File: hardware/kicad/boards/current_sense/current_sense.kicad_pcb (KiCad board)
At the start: 2 copper layers, 120 x 80 mm, 17 parts, among them J1 kanal 1 retur, J2 kanal 2 retur, J3 kanal 3 retur, J4 Arduino, U1 LM358, U2 LM358

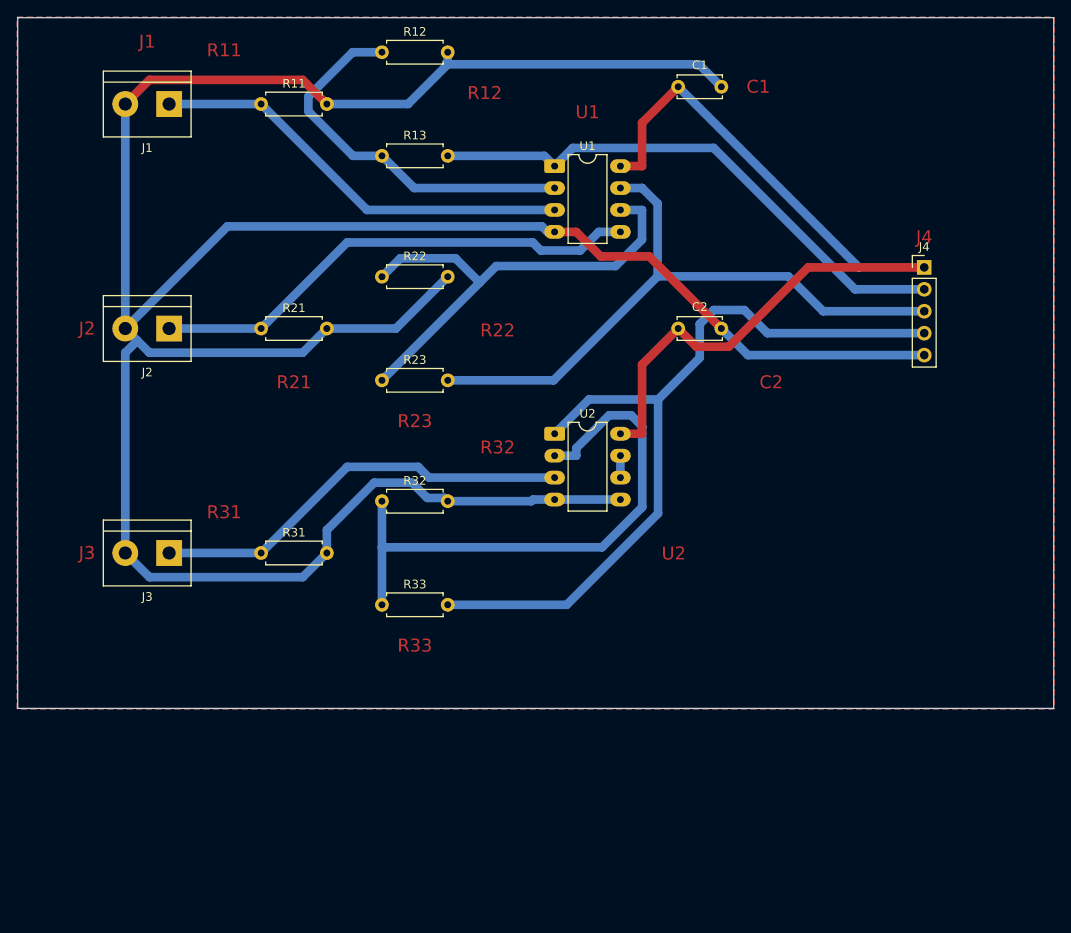
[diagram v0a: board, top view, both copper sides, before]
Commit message: Move all boards to the 104x104 jig format with compact placement
The laser positioning jig takes an exactly 109x109 mm copper blank, so every
board now has identical 104x104 edge cuts (2.5 mm rim). pcb_build.py:
- fixed JIG_W/JIG_H outline, hard failure if content overflows the square
- compact packing: 5 mm bbox gaps (was 8), squarish component cluster below
  the connector zone instead of full-width rows
- mppt/current_sense PLACE layouts re-arranged for the square and tightened

All 7 boards rerouted: 0 unconnected, 0 real DRC errors, and no vias needed
anywhere (the square format routes better than the old elongated boards).
Production DXF/gerbers re-exported; README run-plan updated for the jig
(cut blanks to exactly 109x109, all boards share the same size now).
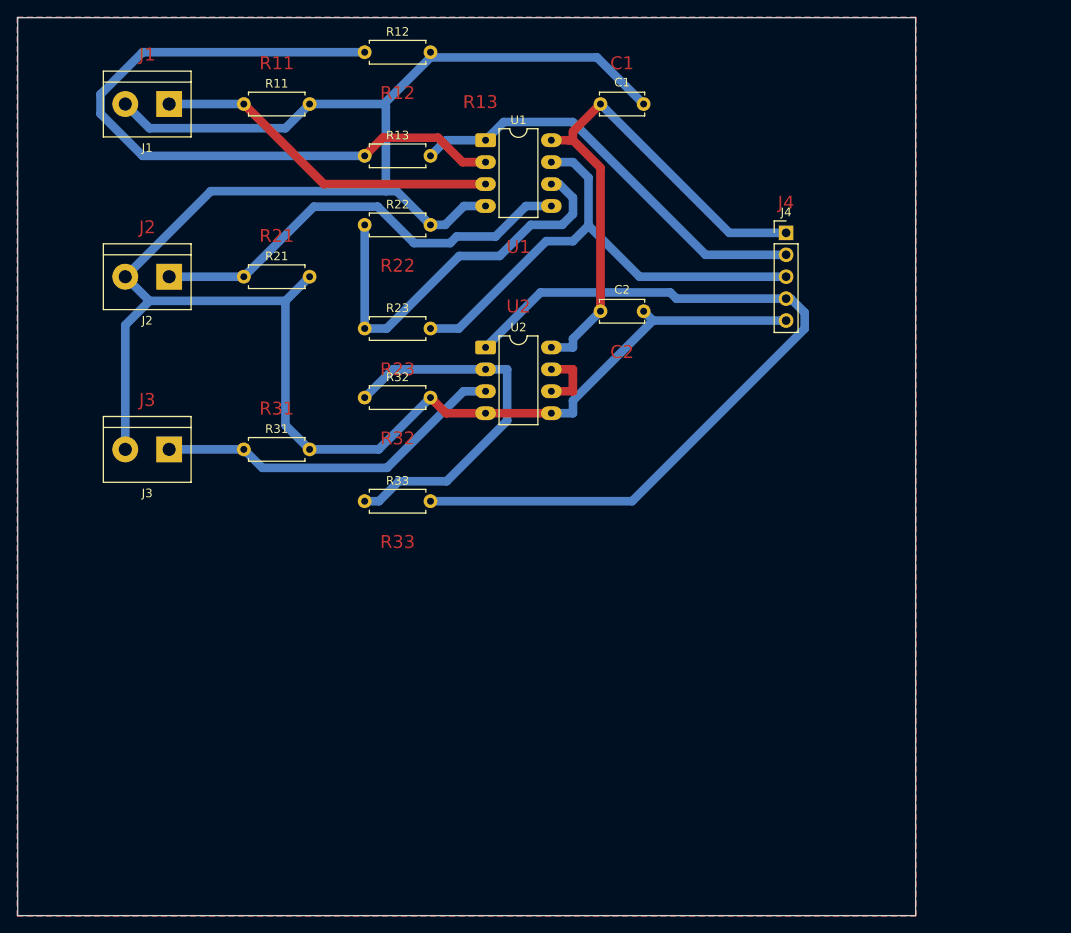
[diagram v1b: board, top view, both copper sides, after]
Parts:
- moved J4 16.5 mm to (109.0, 44.9)
- moved U2 12.8 mm to (74.2, 58.2)
- moved R31 12.2 mm to (46.2, 70.0)
- moved R32 12.2 mm to (60.2, 64.0)
- moved R33 12.2 mm to (60.2, 76.0)
- moved J3 12.0 mm to (37.5, 70.0)
- moved C1 9.22 mm to (87.5, 30.0)
- moved C2 9.22 mm to (87.5, 54.0)
- moved U1 8.54 mm to (74.2, 34.2)
- moved R21 6.32 mm to (46.2, 50.0)
- moved R22 6.32 mm to (60.2, 44.0)
- moved R23 6.32 mm to (60.2, 56.0)
- moved J2 6.00 mm to (37.5, 50.0)
- moved R11 2.00 mm to (46.2, 30.0)
- moved R12 2.00 mm to (60.2, 24.0)
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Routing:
- net GND: track 338.3 -> 251.6 mm
- net /FB1: track 44.6 -> 83.5 mm
- net +5V: track 100.2 -> 64.8 mm
- net /FB3: track 66.5 -> 44.2 mm
- net /I_SENSE2: track 75.3 -> 59.2 mm
- net /I_SENSE1: track 63.3 -> 49.2 mm
- net /FB2: track 56.2 -> 46.7 mm
- net /RET1: track 49.7 -> 40.5 mm
- net /RET3: track 49.3 -> 41.2 mm
- net /RET2: track 57.7 -> 51.2 mm
- net /U2B_FB: track 2.54 -> 7.54 mm
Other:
- board size 120 x 80 mm -> 104 x 104 mm
- board text added: "R13"

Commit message: Condense and center all boards in the jig outline; reroute drive_circuit
Placement (pcb_build.py): connector columns now hug the component block
instead of sitting at the board edges, and the whole cluster is translated to
the center of the 104x104 outline - nothing sits next to the edge cuts
anymore. Fail-hard check if a cluster outgrows the jig.

drive_circuit keeps the hand-made GUI placement but is rerouted with the
two-stage flow: 43 top tracks + 1 via from the GUI autoroute down to 20
pin-to-pin bridges, no via. New tools/strip_routing.py removes existing
routing textually (sexpdata) - in-process pcbnew Remove() access-violates.

All 7 boards: 0 unconnected, 0 real DRC errors, no vias anywhere; buck is
now fully single-sided (0 top tracks). Production files re-exported.
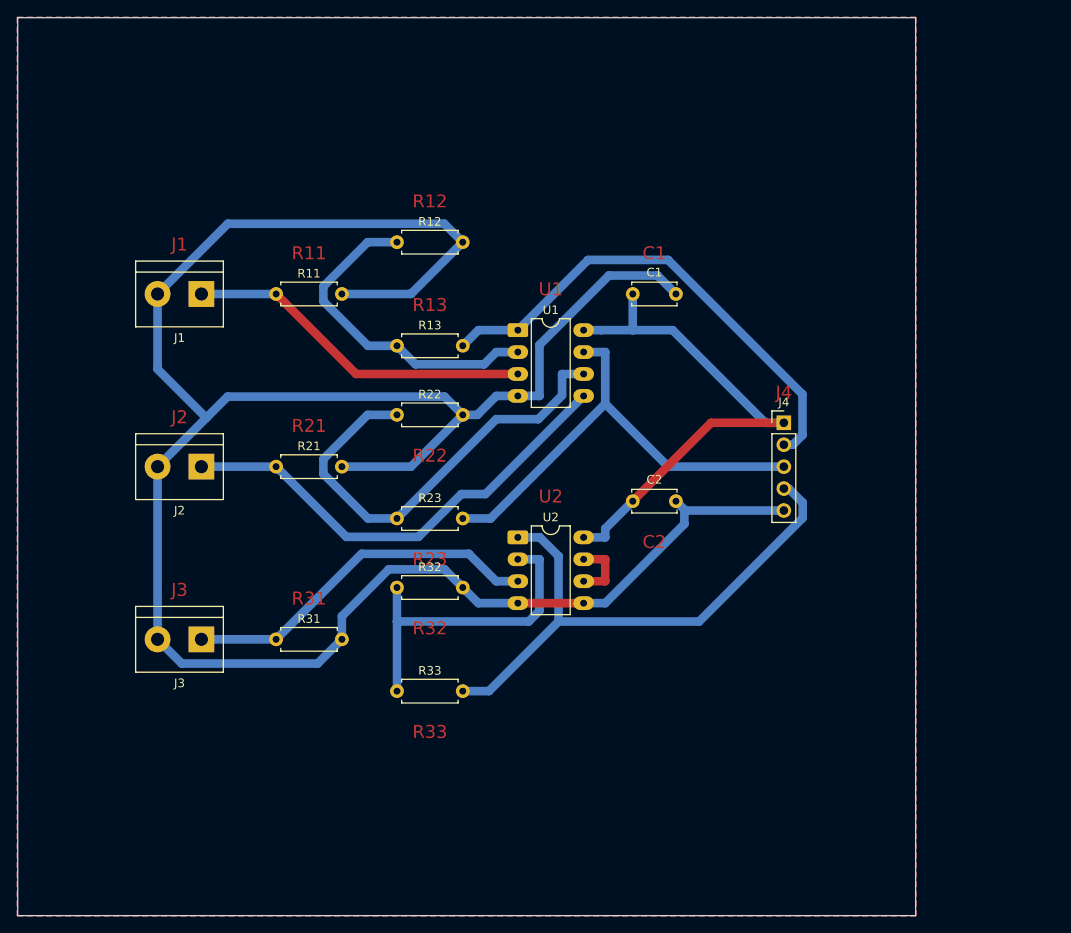
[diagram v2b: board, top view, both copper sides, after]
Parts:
- moved U1 22.3 mm to (77.9, 56.2)
- moved U2 22.3 mm to (77.9, 80.2)
- moved C1 22.3 mm to (91.2, 52.0)
- moved C2 22.3 mm to (91.2, 76.0)
- moved J1 22.3 mm to (41.3, 52.0)
- moved J2 22.3 mm to (41.3, 72.0)
- moved J3 22.3 mm to (41.3, 92.0)
- moved R11 22.3 mm to (49.9, 52.0)
- moved R12 22.3 mm to (63.9, 46.0)
- moved R13 22.3 mm to (63.9, 58.0)
- moved R21 22.3 mm to (49.9, 72.0)
- moved R22 22.3 mm to (63.9, 66.0)
- moved R23 22.3 mm to (63.9, 78.0)
- moved R31 22.3 mm to (49.9, 92.0)
- moved R32 22.3 mm to (63.9, 86.0)
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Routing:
- net /FB1: track 83.5 -> 38.5 mm
- net /I_SENSE3: track 94.0 -> 65.5 mm
- net GND: track 251.6 -> 272.8 mm
- net /I_SENSE1: track 49.2 -> 57.3 mm
- net /FB3: track 44.2 -> 37.5 mm
- net /FB2: track 46.7 -> 53.0 mm
- net /I_SENSE2: track 59.2 -> 54.2 mm
- net +5V: track 64.8 -> 61.1 mm
- net /RET2: track 51.2 -> 54.4 mm
- net /RET3: track 41.2 -> 42.1 mm
